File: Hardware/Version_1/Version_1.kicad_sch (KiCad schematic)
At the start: 93 parts, among them IC1 W25R256JVEIQ, IC3 TPS62A01DRLR, IC4 TPS62A01DRLR, IC5 TPS62A01DRLR, IC6 LIFCL-40-7BG256C, IC7 IS46TR16128D-125KBLA2, J1 GPIO, J2 52435-2271, J3 Conn_01x05_Pin, J4 52435-2271, U1 CAT24C256, Y1 AK3ADDF1-156.2500T3

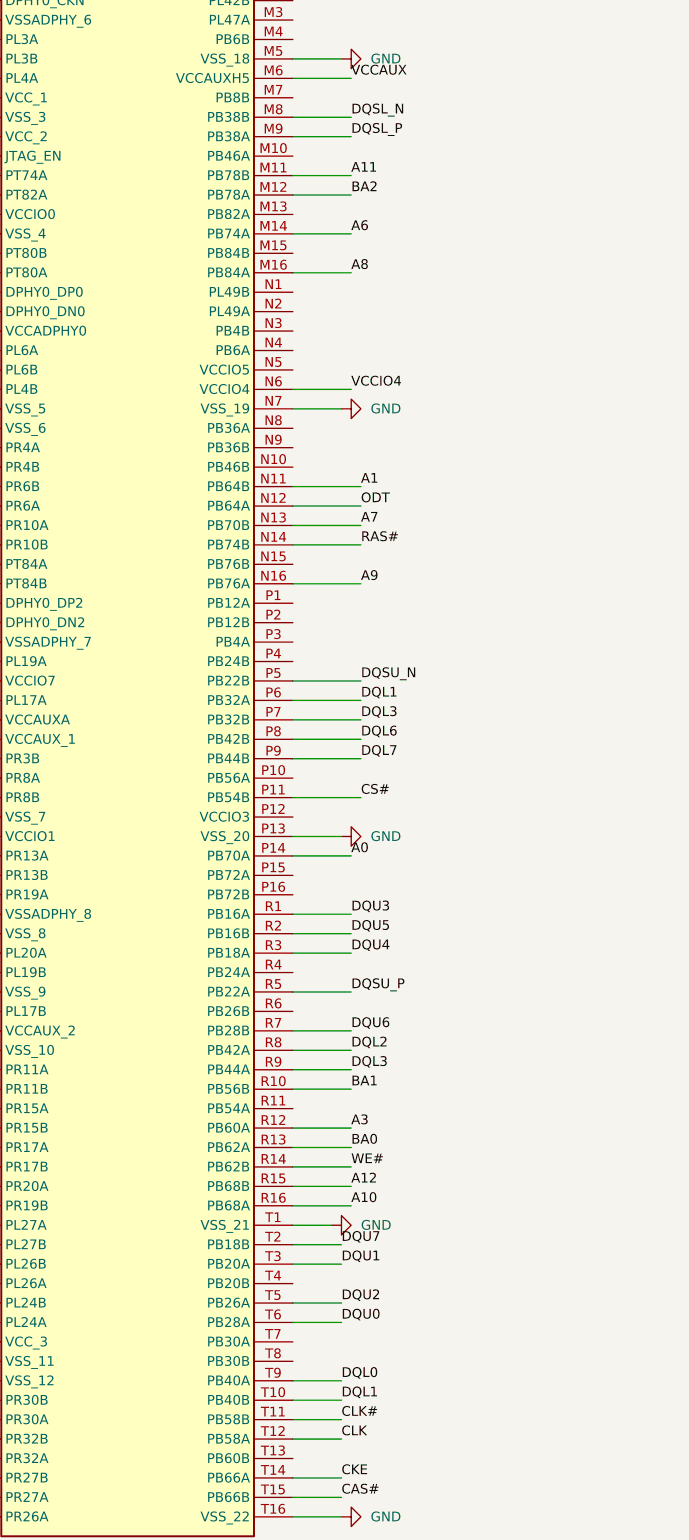
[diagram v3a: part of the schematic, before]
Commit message: Redid routing with custom meadering paramters
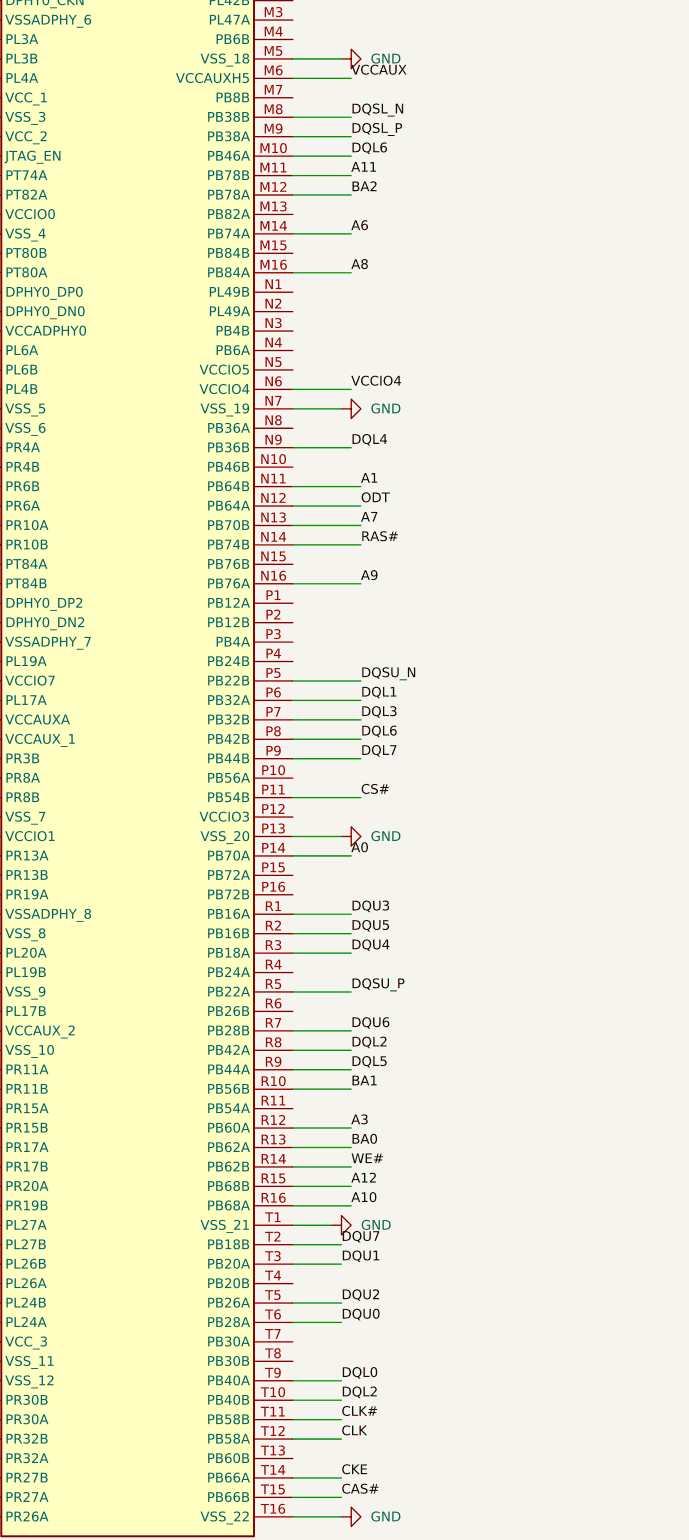
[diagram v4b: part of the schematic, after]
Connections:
- net DQL1: no longer IC6.T10 (PB40B)
- net DQL2: now also IC6.T10 (PB40B)
- net DQL3: no longer IC6.R9 (PB44A)
- net DQL4: now also IC6.N9 (PB36B)
- net DQL5: now also IC6.R9 (PB44A)
- net DQL6: now also IC6.M10 (PB46A)
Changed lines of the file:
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@@
+    (stroke (width 0) (type default))
+  )
+  (wire (pts (xy 398.78 195.58) (xy 406.4 195.58))
     (stroke (width 0) (type default))
   )
@@
   )
   (wire (pts (xy 477.52 162.56) (xy 485.14 162.56))
+    (stroke (width 0) (type default))
+  )
+  (wire (pts (xy 398.78 233.68) (xy 406.4 233.68))
     (stroke (width 0) (type default))
   )
@@
     (effects (font (size 1.27 1.27)) (justify right bottom))
   )
+  (label "DQL4" (at 406.4 233.68 0) (fields_autoplaced)
+    (effects (font (size 1.27 1.27)) (justify left bottom))
+  )
   (label "A6" (at 553.72 331.47 0) (fields_autoplaced)
     (effects (font (size 1.27 1.27)) (justify left bottom))
@@
     (effects (font (size 1.27 1.27)) (justify left bottom))
   )
+  (label "DQL6" (at 406.4 195.58 0) (fields_autoplaced)
+    (effects (font (size 1.27 1.27)) (justify left bottom))
+  )
   (label "CSI2_D2_N" (at 341.63 96.52 0) (fields_autoplaced)
     (effects (font (size 1.27 1.27)) (justify left bottom))
@@
     (effects (font (size 1.27 1.27)) (justify left bottom))
   )
-  (label "DQL3" (at 406.4 314.96 0) (fields_autoplaced)
+  (label "DQL5" (at 406.4 314.96 0) (fields_autoplaced)
     (effects (font (size 1.27 1.27)) (justify left bottom))
   )
@@
     (effects (font (size 1.27 1.27)) (justify left bottom))
   )
-  (label "DQL1" (at 405.13 358.14 0) (fields_autoplaced)
-    (effects (font (size 1.27 1.27)) (justify left bottom))
-  )
+  (label "DQL2" (at 405.13 358.14 0) (fields_autoplaced)
+    (effects (font (size 1.27 1.27)) (justify left bottom))
+  )

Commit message: Started routing DDR address lines
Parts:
- added C46: 100n, Capacitor_SMD:C_0402_1005Metric, symbol Device:C_Small
- renumbered C9 to C1, C17 to C10, C18 to C11, C19 to C12, C20 to C13, C21 to C14, C22 to C15, C23 to C16, C24 to C17, C8 to C18, C32 to C19, C10 to C2, C41 to C20, C42 to C21, C43 to C22, C44 to C23, C45 to C24, C46 to C25, C33 to C26, C37 to C27, C38 to C28, C39 to C29, C11 to C3, C40 to C30, C47 to C31, C48 to C32, C49 to C33, C50 to C34, C51 to C35, C52 to C36, C53 to C37, C28 to C38, C29 to C39, C12 to C4, C30 to C40, C34 to C41, C35 to C42, C36 to C43, C25 to C44, C26 to C45, C27 to C47, C31 to C48, C54 to C49, C13 to C5, C6 to C50, C7 to C51, C4 to C52, C5 to C53, C2 to C54, C3 to C55, C14 to C6, C15 to C7, C1 to C8, C16 to C9, FB6 to FB4, FB4 to FB5, FB5 to FB6, IC6 to IC1, IC1 to IC2, IC7 to IC3, IC5 to IC4, IC3 to IC5, IC4 to IC6, J3 to J2, J2 to J3, L3 to L1, L1 to L3, R11 to R10, R9 to R11, R7 to R12, R8 to R13, R6 to R14, R3 to R15, R4 to R16, R5 to R17, R12 to R3, R13 to R4, R14 to R5, R15 to R6, R17 to R7, R16 to R8, R10 to R9
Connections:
- net CLK is gone; now on net CLK_P: IC1.T12 (PB58A)
- net CLK# is gone; now on net CLK_N: IC1.T11 (PB58B)
- net +1V0: now also IC1.P12 (VCCIO3), C46.1
- net A1: now also IC1.M15 (PB84B); no longer IC1.N11 (PB64B)
- net A10: now also IC1.M13 (PB82A); no longer IC1.R16 (PB68A)
- net A11: now also IC1.T15 (PB66B); no longer IC1.M11 (PB78B)
- net A12: now also IC1.N14 (PB74B); no longer IC1.R15 (PB68B)
- net A13: now also IC1.R16 (PB68A)
- net A2: now also IC1.N15 (PB76B)
- net A3: now also IC1.R14 (PB62B); no longer IC1.R12 (PB60A)
- net A4: now also IC1.T14 (PB66A); no longer IC1.L12 (PB82B)
- net A5: now also IC1.P15 (PB72A); no longer IC1.L11 (PB80A)
- net A6: now also IC1.R15 (PB68B); no longer IC1.M14 (PB74A)
- net A7: now also IC1.N16 (PB76A); no longer IC1.N13 (PB70B)
- net A8: now also IC1.P16 (PB72B); no longer IC1.M16 (PB84A)
- net A9: now also IC1.M16 (PB84A); no longer IC1.N16 (PB76A)
- net BA0: now also IC1.T13 (PB60B); no longer IC1.R13 (PB62A)
- net BA1: now also IC1.M14 (PB74A); no longer IC1.R10 (PB56B)
- net BA2: now also IC1.R13 (PB62A); no longer IC1.M12 (PB78A)
- net CAS#: now also IC1.N12 (PB64A); no longer IC1.T15 (PB66B)
- net CKE: now also IC1.M11 (PB78B); no longer IC1.T14 (PB66A)
- net DQL2: no longer IC1.R8 (PB42A)
- net DQL6: no longer IC1.P8 (PB42B)
- net GND: now also C46.2
- net ODT: now also IC1.N13 (PB70B); no longer IC1.N12 (PB64A)
- net RAS#: now also IC1.N11 (PB64B); no longer IC1.N14 (PB74B)
- net WE#: now also IC1.L12 (PB82B); no longer IC1.R14 (PB62B)
- net CK renamed CLK_P
- net CK# renamed CLK_N
